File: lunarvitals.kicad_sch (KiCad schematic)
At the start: 38 parts, among them J1 ConductiveCord, J2 MPU6050, J3 SEN11574, J5 USB_C_Receptacle_PowerOnly_6P, J6 Battery, Q1 FS8205, U1 NRF52840-DONGLE, U2 BMP280, U3 AP2112K-3.3, U4 TP4056, U5 MLX90614ESF-AAA-000-TU, U6 DW01A

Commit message: include connectors in BOM
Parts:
- J2, J3: now in the parts list
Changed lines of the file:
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@@
 		(unit 1)
 		(exclude_from_sim no)
-		(in_bom no)
+		(in_bom yes)
 		(on_board yes)
 		(dnp no)
@@
 		(unit 1)
 		(exclude_from_sim no)
-		(in_bom no)
+		(in_bom yes)
 		(on_board yes)
 		(dnp no)

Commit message: final updates to PCB
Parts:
- removed D3: Blue_LED, LED_SMD:LED_0603_1608Metric, symbol Device:LED
- removed R6: 330, Resistor_SMD:R_0402_1005Metric, symbol Device:R
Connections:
- net B-: now also J6.1 (Pin_1); no longer J6.2 (Pin_2)
- net BOut+: now also J6.2 (Pin_2); no longer J6.1 (Pin_1)
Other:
- moved on the sheet: D4, J3, J6, R1, R2, R4

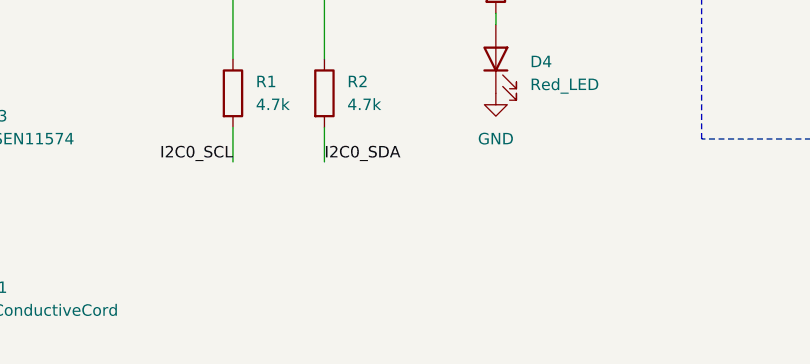
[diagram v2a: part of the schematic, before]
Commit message: added connector for MAX30102
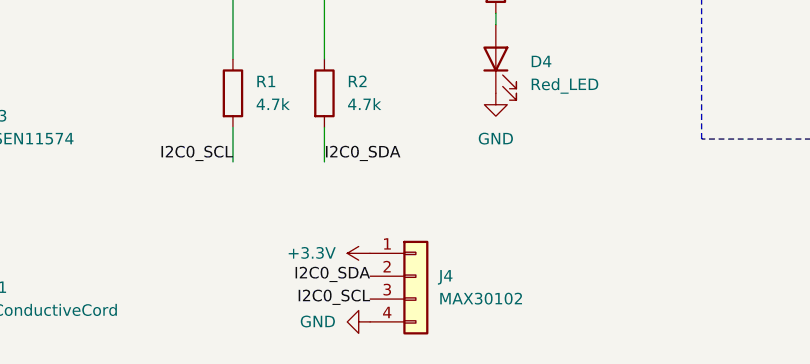
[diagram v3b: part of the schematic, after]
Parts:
- added J4: MAX30102, Connector_JST:JST_XH_B4B-XH-A_1x04_P2.50mm_Vertical, symbol Connector_Generic:Conn_01x04
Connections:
- net +3.3V: now also J4.1 (Pin_1)
- net GND: now also J4.4 (Pin_4)
- net I2C0_SCL: now also J4.3 (Pin_3)
- net I2C0_SDA: now also J4.2 (Pin_2)
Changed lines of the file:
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@@
 		)
 	)
+	(label "I2C0_SCL"
+		(at 140.97 181.61 180)
+		(effects
+			(font
+				(size 1.27 1.27)
+			)
+			(justify right)
+		)
+	)
 	(label "I2C1_SCL"
 		(at 157.48 66.04 0)
@@
 		)
 	)
+	(label "I2C0_SDA"
+		(at 140.97 179.07 180)
+		(effects
+			(font
+				(size 1.27 1.27)
+			)
+			(justify right)
+		)
+	)
 	(label "I2C0_SCL"
 		(at 22.86 157.48 180)
@@
 	)
 	(symbol
+		(lib_id "power:GND")
+		(at 140.97 184.15 270)
+		(unit 1)
+		(exclude_from_sim no)
+		(in_bom yes)
+		(on_board yes)
+		(dnp no)
+		(fields_autoplaced yes)
+		(property "Reference" "#PWR020"
+			(at 134.62 184.15 0)
+			(effects
+				(font
+					(size 1.27 1.27)
+				)
+				(hide yes)
+			)
+		)
+		(property "Value" "GND"
+			(at 137.16 184.1499 90)
+			(effects
+				(font
+					(size 1.27 1.27)
+				)
+				(justify right)
+			)
+		)
+		(property "Footprint" ""
+			(at 140.97 184.15 0)
+			(effects
+				(font
+					(size 1.27 1.27)
+				)
+				(hide yes)
+			)
+		)
+		(property "Datasheet" ""
+			(at 140.97 184.15 0)
+			(effects
+				(font
+					(size 1.27 1.27)
+				)
+				(hide yes)
+			)
+		)
+		(property "Description" "Power symbol creates a global label with name \"GND\" , ground"
+			(at 140.97 184.15 0)
+			(effects
+				(font
+					(size 1.27 1.27)
+				)
+				(hide yes)
+			)
+		)
+		(pin "1"
+		)
+		(instances
+			(project "lunarvitals"
+				(path "/5743f844-2fd9-4187-922b-f2fa73d8e73e"
+					(reference "#PWR020")
+					(unit 1)
+				)
+			)
+		)
+	)
+	(symbol
 		(lib_id "Connector_Generic:Conn_01x04")
 		(at 38.1 180.34 0)
@@
 	)
 	(symbol
+		(lib_id "Connector_Generic:Conn_01x04")
+		(at 146.05 179.07 0)
+		(unit 1)
+		(exclude_from_sim no)
+		(in_bom yes)
+		(on_board yes)
+		(dnp no)
+		(fields_autoplaced yes)
+		(property "Reference" "J4"
+			(at 148.59 179.0699 0)
+			(effects
+				(font
+					(size 1.27 1.27)
+				)
+				(justify left)
+			)
+		)
+		(property "Value" "MAX30102"
+			(at 148.59 181.6099 0)
+			(effects
+				(font
+					(size 1.27 1.27)
+				)
+				(justify left)
+			)
+		)
+		(property "Footprint" "Connector_JST:JST_XH_B4B-XH-A_1x04_P2.50mm_Vertical"
+			(at 146.05 179.07 0)
+			(effects
+				(font
+					(size 1.27 1.27)
+				)
+				(hide yes)
+			)
+		)
+		(property "Datasheet" "~"
+			(at 146.05 179.07 0)
+			(effects
+				(font
+					(size 1.27 1.27)
+				)
+				(hide yes)
+			)
+		)
+		(property "Description" "JST XA Header Through-hole type"
+			(at 146.05 179.07 0)
+			(effects
+				(font
+					(size 1.27 1.27)
+				)
+				(hide yes)
+			)
+		)
+		(property "LCSC" "C144395"
+			(at 146.05 179.07 0)
+			(effects
+				(font
+					(size 1.27 1.27)
+				)
+				(hide yes)
+			)
+		)
+		(pin "2"
+		)
+		(pin "1"
+		)
+		(pin "4"
+		)
+		(pin "3"
+		)
+		(instances
+			(project "lunarvitals"
+				(path "/5743f844-2fd9-4187-922b-f2fa73d8e73e"
+					(reference "J4")
+					(unit 1)
+				)
+			)
+		)
+	)
+	(symbol
 		(lib_id "power:+3.3V")
 		(at 30.48 101.6 0)
@@
 					(unit 1)
 				)
+			)
+		)
+	)
+	(symbol
+		(lib_id "power:+3.3V")
+		(at 140.97 176.53 90)
+		(unit 1)
+		(exclude_from_sim no)
+		(in_bom yes)
+		(on_board yes)
+		(dnp no)
+		(fields_autoplaced yes)
+		(property "Reference" "#PWR012"
+			(at 144.78 176.53 0)
+			(effects
+				(font
+					(size 1.27 1.27)
+				)
+				(hide yes)
+			)
+		)
+		(property "Value" "+3.3V"
+			(at 137.16 176.5299 90)
+			(effects
+				(font
+					(size 1.27 1.27)
+				)
+				(justify left)
+			)
+		)
+		(property "Footprint" ""
+			(at 140.97 176.53 0)
+			(effects
+				(font
+					(size 1.27 1.27)
+				)
+				(hide yes)
+			)
+		)
+		(property "Datasheet" ""
+			(at 140.97 176.53 0)
+			(effects
+				(font
+					(size 1.27 1.27)
+				)
+				(hide yes)
+			)
+		)
+		(property "Description" "Power symbol creates a global label with name \"+3.3V\""
+			(at 140.97 176.53 0)
+			(effects
+				(font
+					(size 1.27 1.27)
+				)
+				(hide yes)
+			)
+		)
+		(pin "1"
+		)
+		(instances
+			(project "lunarvitals"
+				(path "/5743f844-2fd9-4187-922b-f2fa73d8e73e"
+					(reference "#PWR012")
+					(unit 1)
+				)

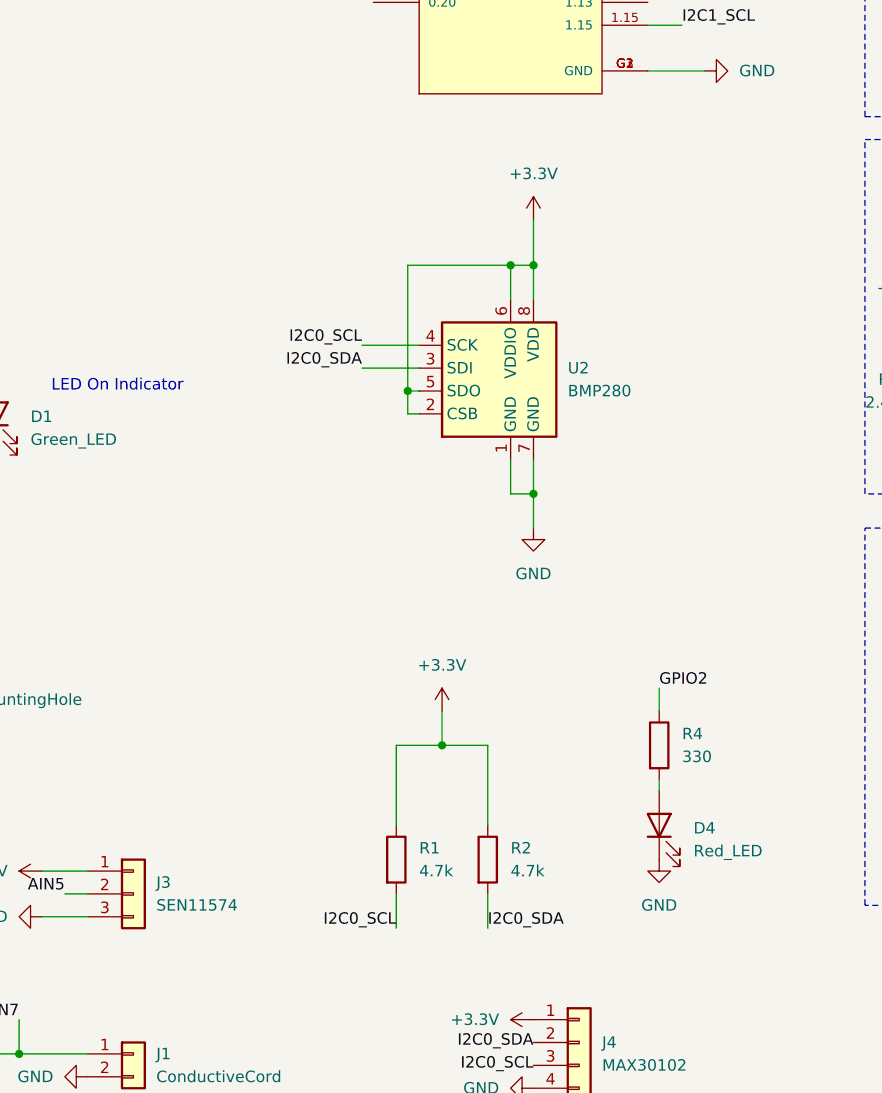
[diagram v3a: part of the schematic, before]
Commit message: bmp breakout board changes (unfinished)
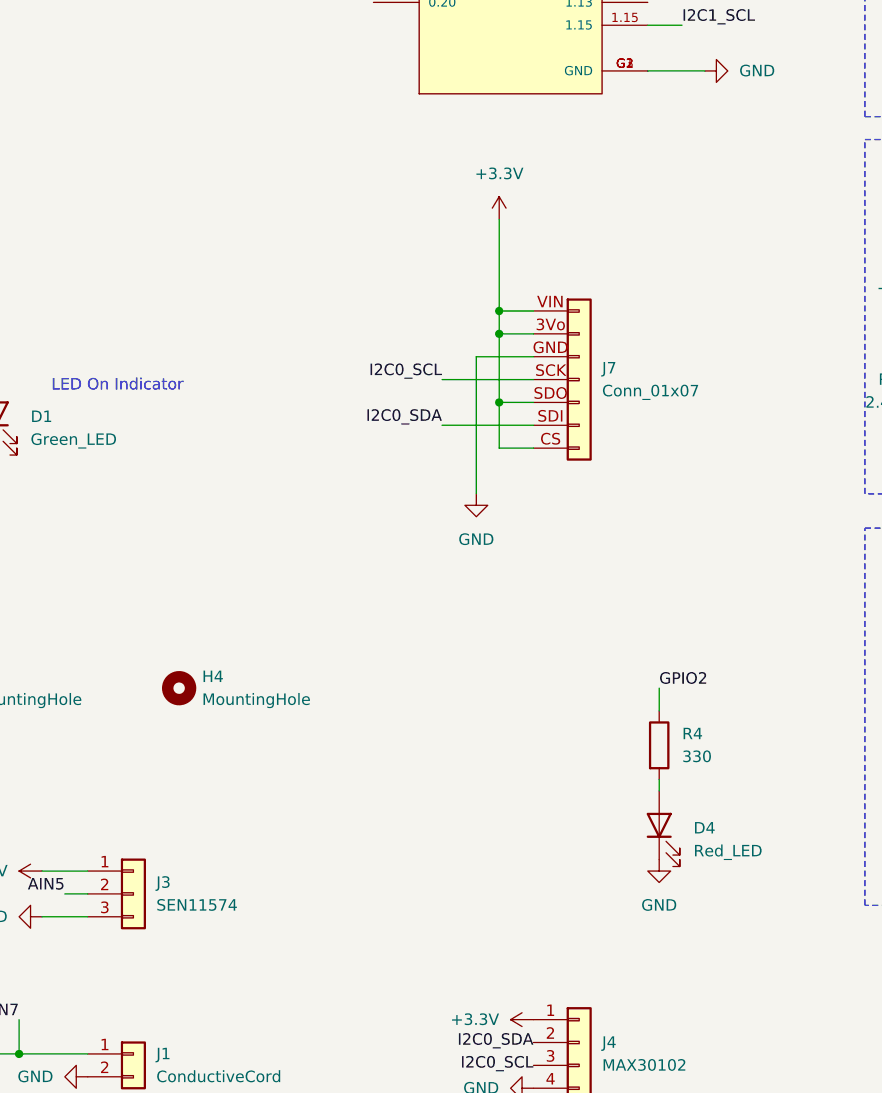
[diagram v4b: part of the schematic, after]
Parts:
- removed R1, R2: 4.7k, Resistor_SMD:R_0402_1005Metric, symbol Device:R
- removed U2: BMP280, Package_LGA:Bosch_LGA-8_2x2.5mm_P0.65mm_ClockwisePinNumbering, symbol Sensor_Pressure:BMP280
- added H4: MountingHole, MountingHole:MountingHole_2.2mm_M2, symbol Mechanical:MountingHole
- added J7: Conn_01x07, lunar_vitals_custom:bmp280breakout, symbol Connector_Generic:Conn_01x07
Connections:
- net +3.3V: now also J7.3Vo (Pin_2), J7.CS (Pin_7), J7.SDO (Pin_5), J7.VIN (Pin_1)
- net GND: now also J7.GND (Pin_3)
- net I2C0_SCL: now also J7.SCK (Pin_4)
- net I2C0_SDA: now also J7.SDI (Pin_6)

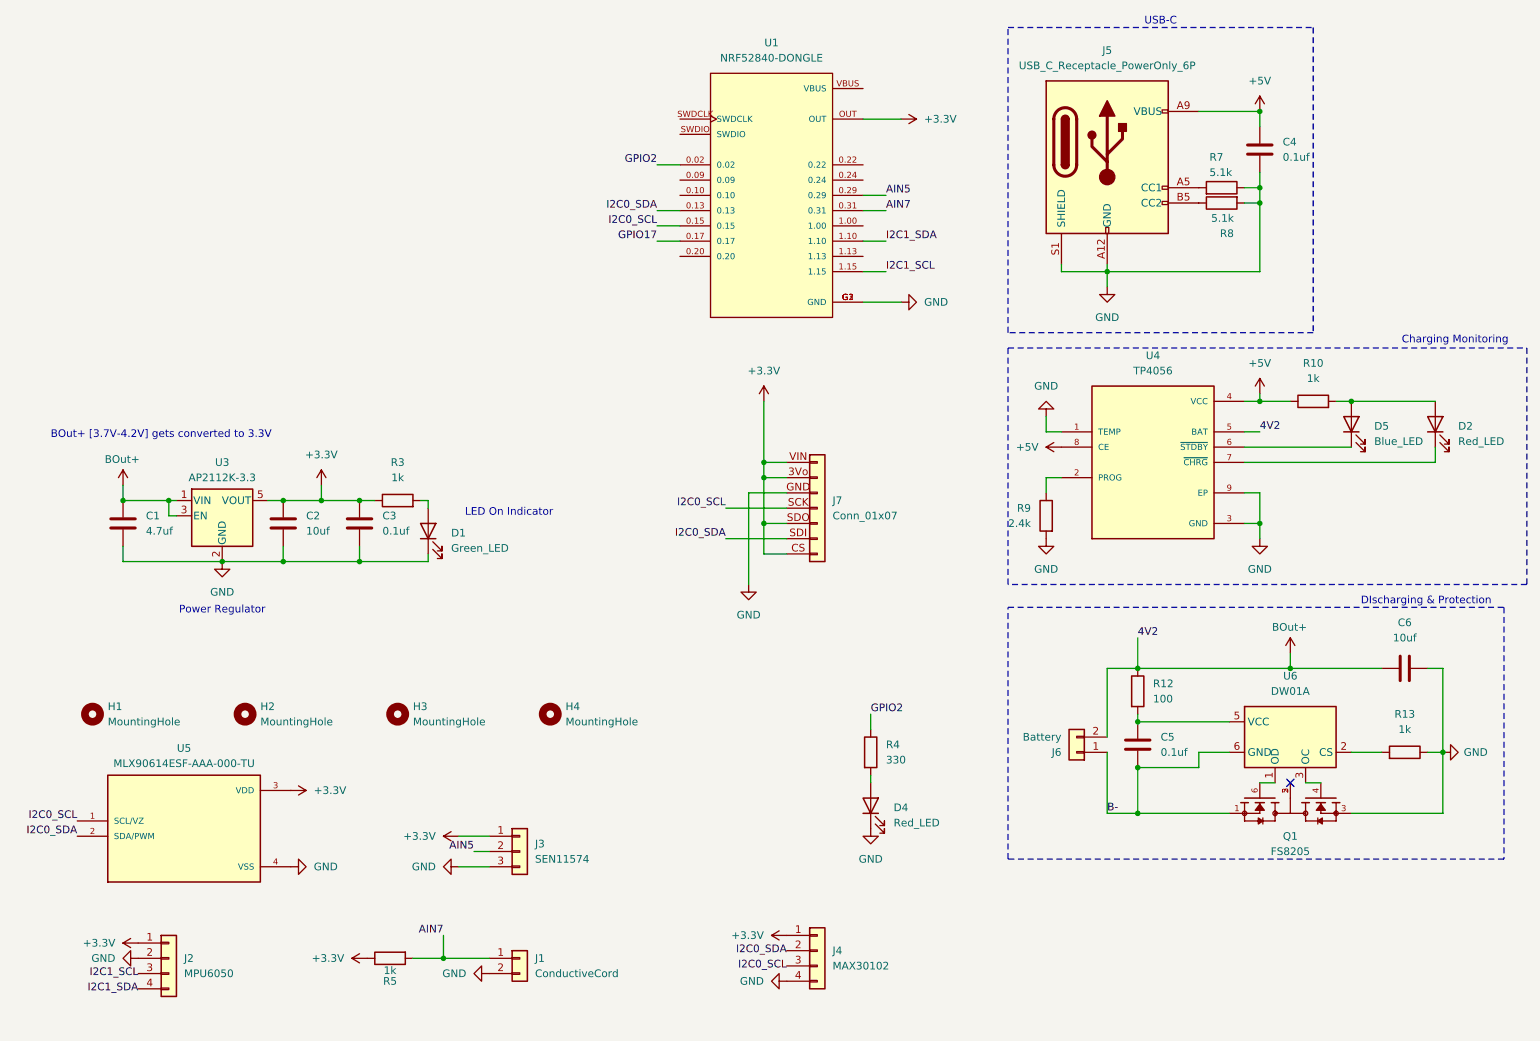
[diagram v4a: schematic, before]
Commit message: LED changes and BMP model
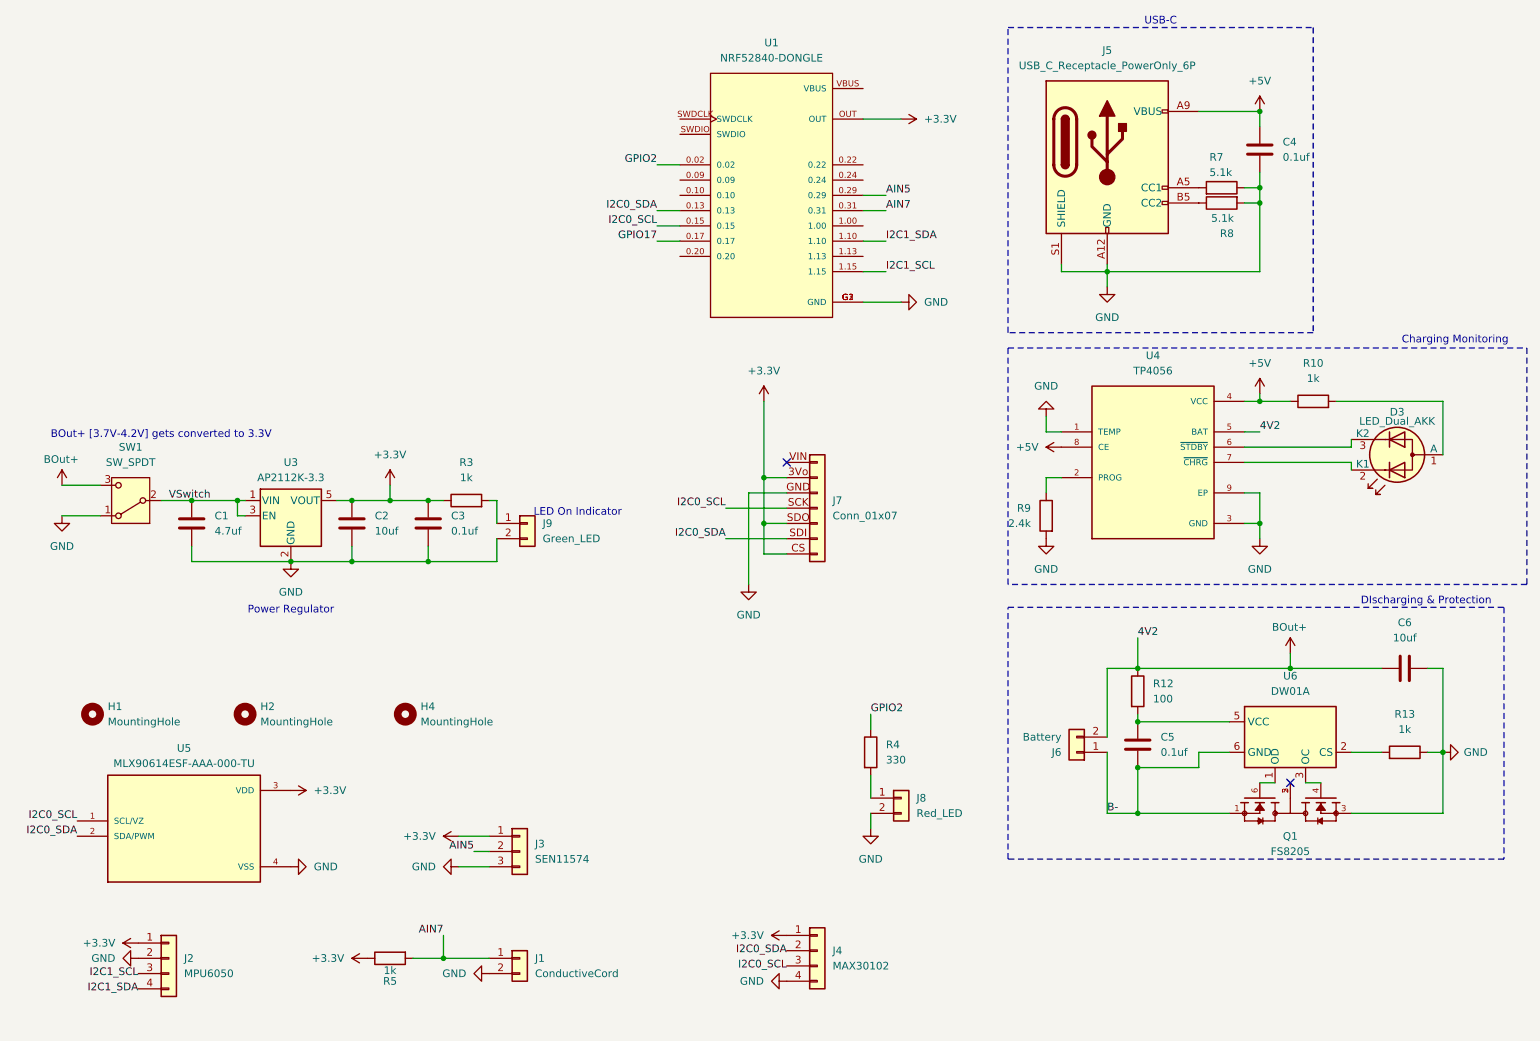
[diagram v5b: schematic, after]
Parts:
- removed D1: Green_LED, LED_SMD:LED_0603_1608Metric, symbol Device:LED
- removed D2, D4: Red_LED, LED_SMD:LED_0603_1608Metric, symbol Device:LED
- removed D5: Blue_LED, LED_SMD:LED_0603_1608Metric, symbol Device:LED
- removed H3: MountingHole, MountingHole:MountingHole_2.2mm_M2, symbol Mechanical:MountingHole
- added D3: LED_Dual_AKK, lunar_vitals_custom:KB APBA3010SURKCGKC-GX, symbol Device:LED_Dual_KAK
- added J8: Red_LED, Connector_PinSocket_2.54mm:PinSocket_1x02_P2.54mm_Vertical, symbol Connector_Generic:Conn_01x02
- added J9: Green_LED, Connector_PinSocket_2.54mm:PinSocket_1x02_P2.54mm_Vertical, symbol Connector_Generic:Conn_01x02
- added SW1: SW_SPDT, Button_Switch_THT:SW_Slide_SPDT_Angled_CK_OS102011MA1Q, symbol Switch:SW_SPDT
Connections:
- net +3.3V: no longer J7.VIN (Pin_1)
- net BOut+: now also SW1.3 (C); no longer C1.1, U3.1 (VIN), U3.3 (EN)
- net GND: now also J8.2 (Pin_2), J9.2 (Pin_2), SW1.1 (A)
- net at R10.2: now also D3.1 (A)
- net at R4.2: now also J8.1 (Pin_1)
- net at U4.6 (~{STDBY}): now also D3.3 (K2)
- net at U4.7 (~{CHRG}): now also D3.2 (K1)
- net at R3.2: now also J9.1 (Pin_1)
- new net VSwitch: C1.1, SW1.2 (B), U3.1 (VIN), U3.3 (EN)
- no-connect marks 1 -> 2
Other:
- moved on the sheet: C1, C2, C3, H4, R3, U3

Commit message: final changes
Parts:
- removed J8: Red_LED, Connector_PinSocket_2.54mm:PinSocket_1x02_P2.54mm_Vertical, symbol Connector_Generic:Conn_01x02
- removed J9: Green_LED, Connector_PinSocket_2.54mm:PinSocket_1x02_P2.54mm_Vertical, symbol Connector_Generic:Conn_01x02
- added D1: Green_LED, LED_THT:LED_D3.0mm, symbol Device:LED
- added D2: Red_LED, LED_THT:LED_D3.0mm, symbol Device:LED
- added JP1: Jumper_2_Small_Open, TestPoint:TestPoint_2Pads_Pitch2.54mm_Drill0.8mm, symbol Jumper:Jumper_2_Small_Open
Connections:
- net +5V: now also JP1.2 (B)
- net BOut+: now also C1.1, U3.1 (VIN)
- net GND: now also D1.1 (K), D2.1 (K)
- net VSwitch: no longer C1.1, SW1.2 (B), U3.1 (VIN), U3.3 (EN)
- net at U1.VBUS: now also JP1.1 (A)
- net at R4.2: now also D2.2 (A)
- net at R3.2: now also D1.2 (A)
- new net: SW1.2 (B), U3.3 (EN)
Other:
- moved on the sheet: C1, R4, SW1

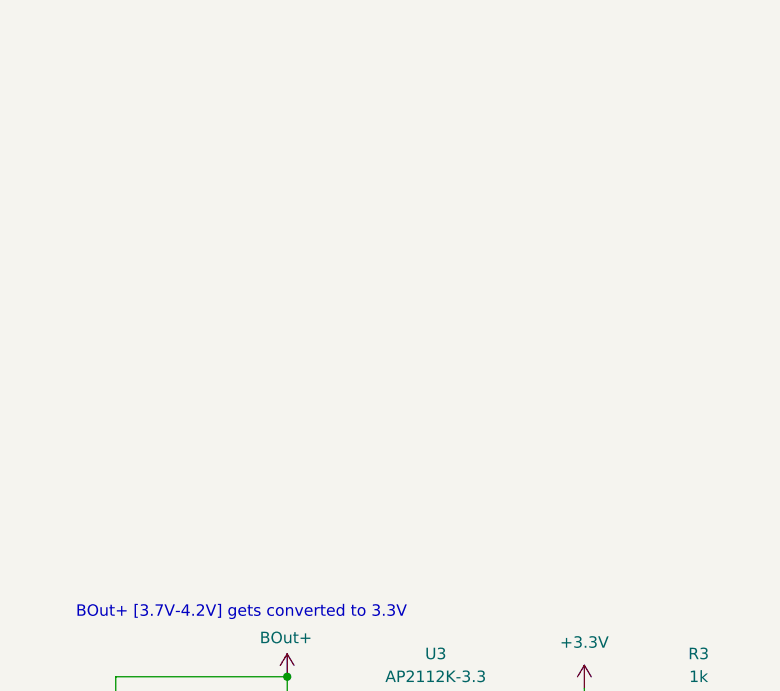
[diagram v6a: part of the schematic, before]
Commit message: added unpopulated pullup resistors for I2C
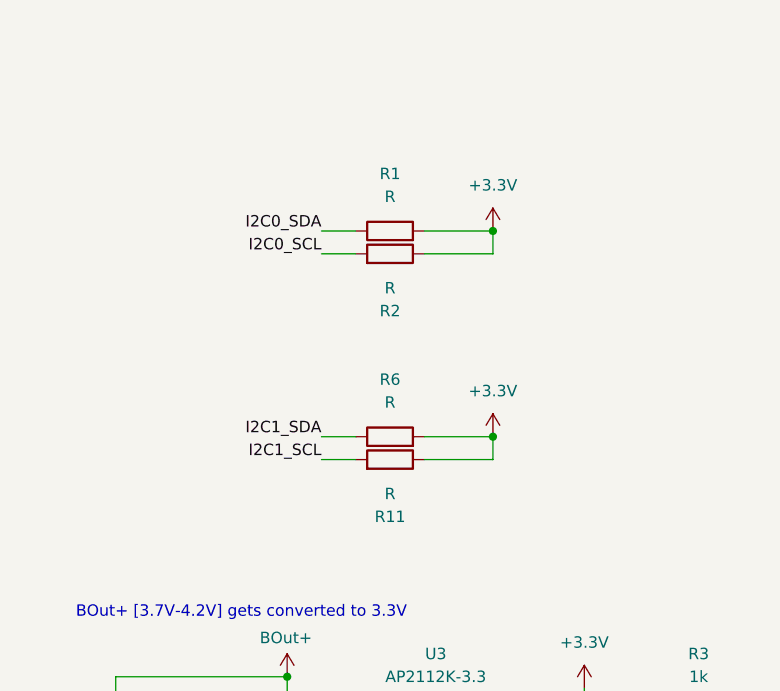
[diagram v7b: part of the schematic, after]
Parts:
- added R1, R11, R2, R6: R, Resistor_SMD:R_0805_2012Metric_Pad1.20x1.40mm_HandSolder, symbol Device:R
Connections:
- net +3.3V: now also R1.2, R11.1, R2.1, R6.2
- net I2C0_SCL: now also R2.2
- net I2C0_SDA: now also R1.1
- net I2C1_SCL: now also R11.2
- net I2C1_SDA: now also R6.1

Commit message: fix jumper footprint and adjust charge indication led
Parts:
- JP1: footprint TestPoint:TestPoint_2Pads_Pitch2.54mm_Drill0.8mm -> Jumper:SolderJumper-2_P1.3mm_Open_RoundedPad1.0x1.5mm
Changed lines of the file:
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@@
 			)
 		)
-		(property "Footprint" "TestPoint:TestPoint_2Pads_Pitch2.54mm_Drill0.8mm"
+		(property "Footprint" "Jumper:SolderJumper-2_P1.3mm_Open_RoundedPad1.0x1.5mm"
 			(at 157.48 35.56 0)
 			(effects
